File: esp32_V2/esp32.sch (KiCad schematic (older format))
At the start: 71 parts, among them IC1 KF33BD-TR, J1 USB_C, J2 Conn_01x26, J3 Conn_01x26, J4 pH, J5 ORP, Q2 8205A, Q3 BC817, Q4 BC817, SW1 Reset, SW2 Boot, U1 CH340G, U2 TC4056, U3 DW01A, U4 LM358, U5 TLC272, U6 LM358, X1 12 MHz

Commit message: Remove V2 folder and rename V2.1 folder to V2
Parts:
- removed IC1: KF33BD-TR, Package_SO:SO-8_3.9x4.9mm_P1.27mm, symbol KF33BDT-TR:KF33BD-TR
- added IC1: KF33BD-TR, Package_SO:SO-8_3.9x4.9mm_P1.27mm, symbol esp32-rescue:KF33BD-TR-KF33BDT-TR
- added JP10, JP11, JP13, JP6, JP9: Jumper_NO, Connector_PinSocket_2.54mm:PinSocket_1x02_P2.54mm_Vertical, symbol Device:Jumper_NO_Small
- J1: symbol USB_C_Receptacle_2.0:USB_C_Receptacle_2.0 -> esp32-rescue:USB_C_Receptacle_2.0-USB_C_Receptacle_2.0
- Q2: symbol 8205A:8205A -> esp32-rescue:8205A-8205A
- U3: symbol DW01A:DW01A -> esp32-rescue:DW01A-DW01A
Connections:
- net 28: now also JP9.1
- net 29: now also JP10.1
- net Bat: now also ESP32.6 (IO34), JP13.1; no longer ESP32.9 (IO33), R15.2, R16.1
- net GND: now also IC1.2 (GND), IC1.3 (GND), IC1.6 (GND), IC1.7 (GND), JP10.2, JP9.2
- net Temp: now also ESP32.9 (IO33); no longer ESP32.7 (IO35)
- net VBUS: now also JP6.2; no longer J1.A4-B9 (VBUS), J1.B4-A9 (VBUS)
- net Vcc: now also JP11.2; no longer ESP32.10 (IO25)
- net pH: now also ESP32.7 (IO35); no longer ESP32.6 (IO34)
- net at C9.1, JP2.1: now also IC1.1 (Vout)
- net at C8.1, JP1.1: now also IC1.8 (Vin)
- new net: ESP32.10 (IO25), JP11.1
- new net: JP13.2, R15.2, R16.1
- new net: J1.A4-B9 (VBUS), J1.B4-A9 (VBUS), JP6.1
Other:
- moved on the sheet: R19, R26, U4B, U5B, U5C

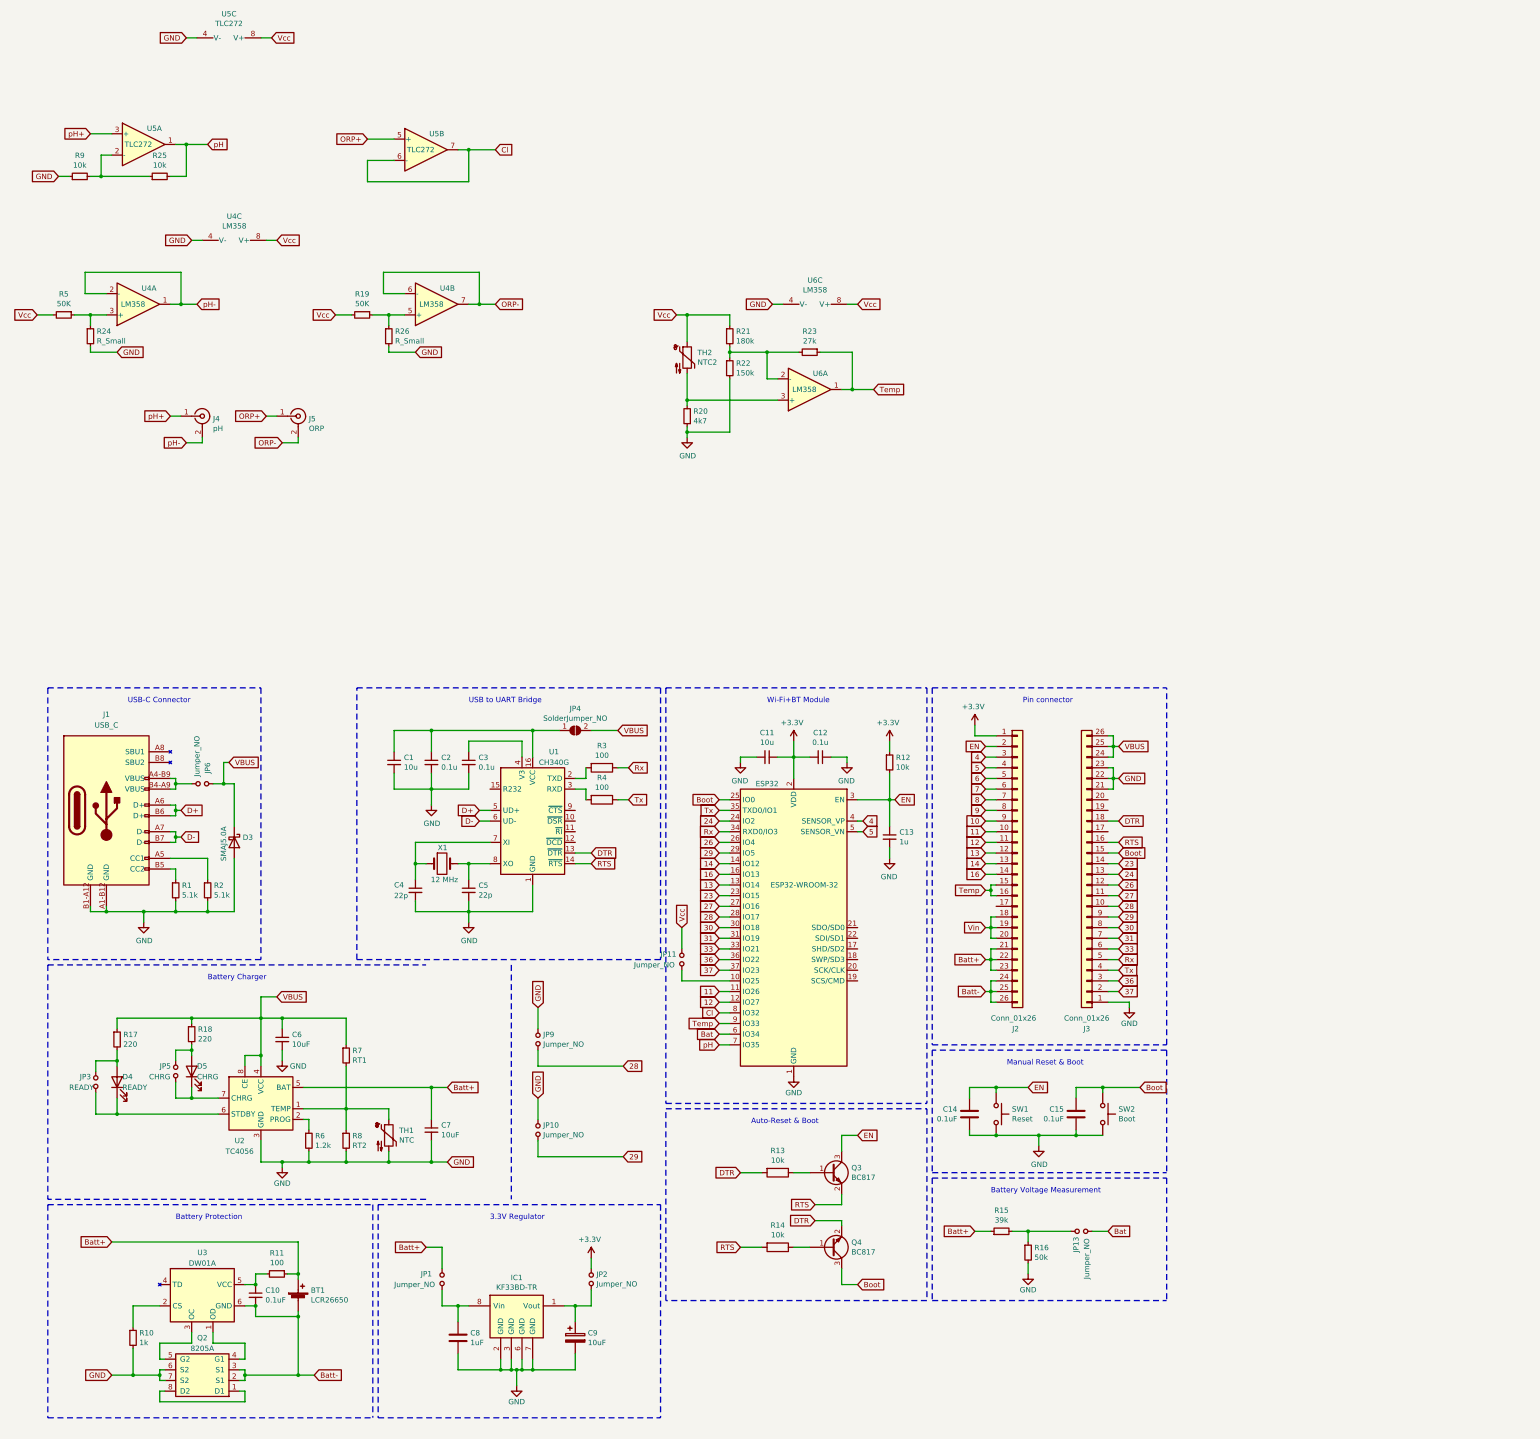
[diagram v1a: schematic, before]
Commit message: 1) Correct components values in measurement circuits - 2) Schematic cleanup - 3) Fix tracks in PCB - 4) Add Thermistor calculator
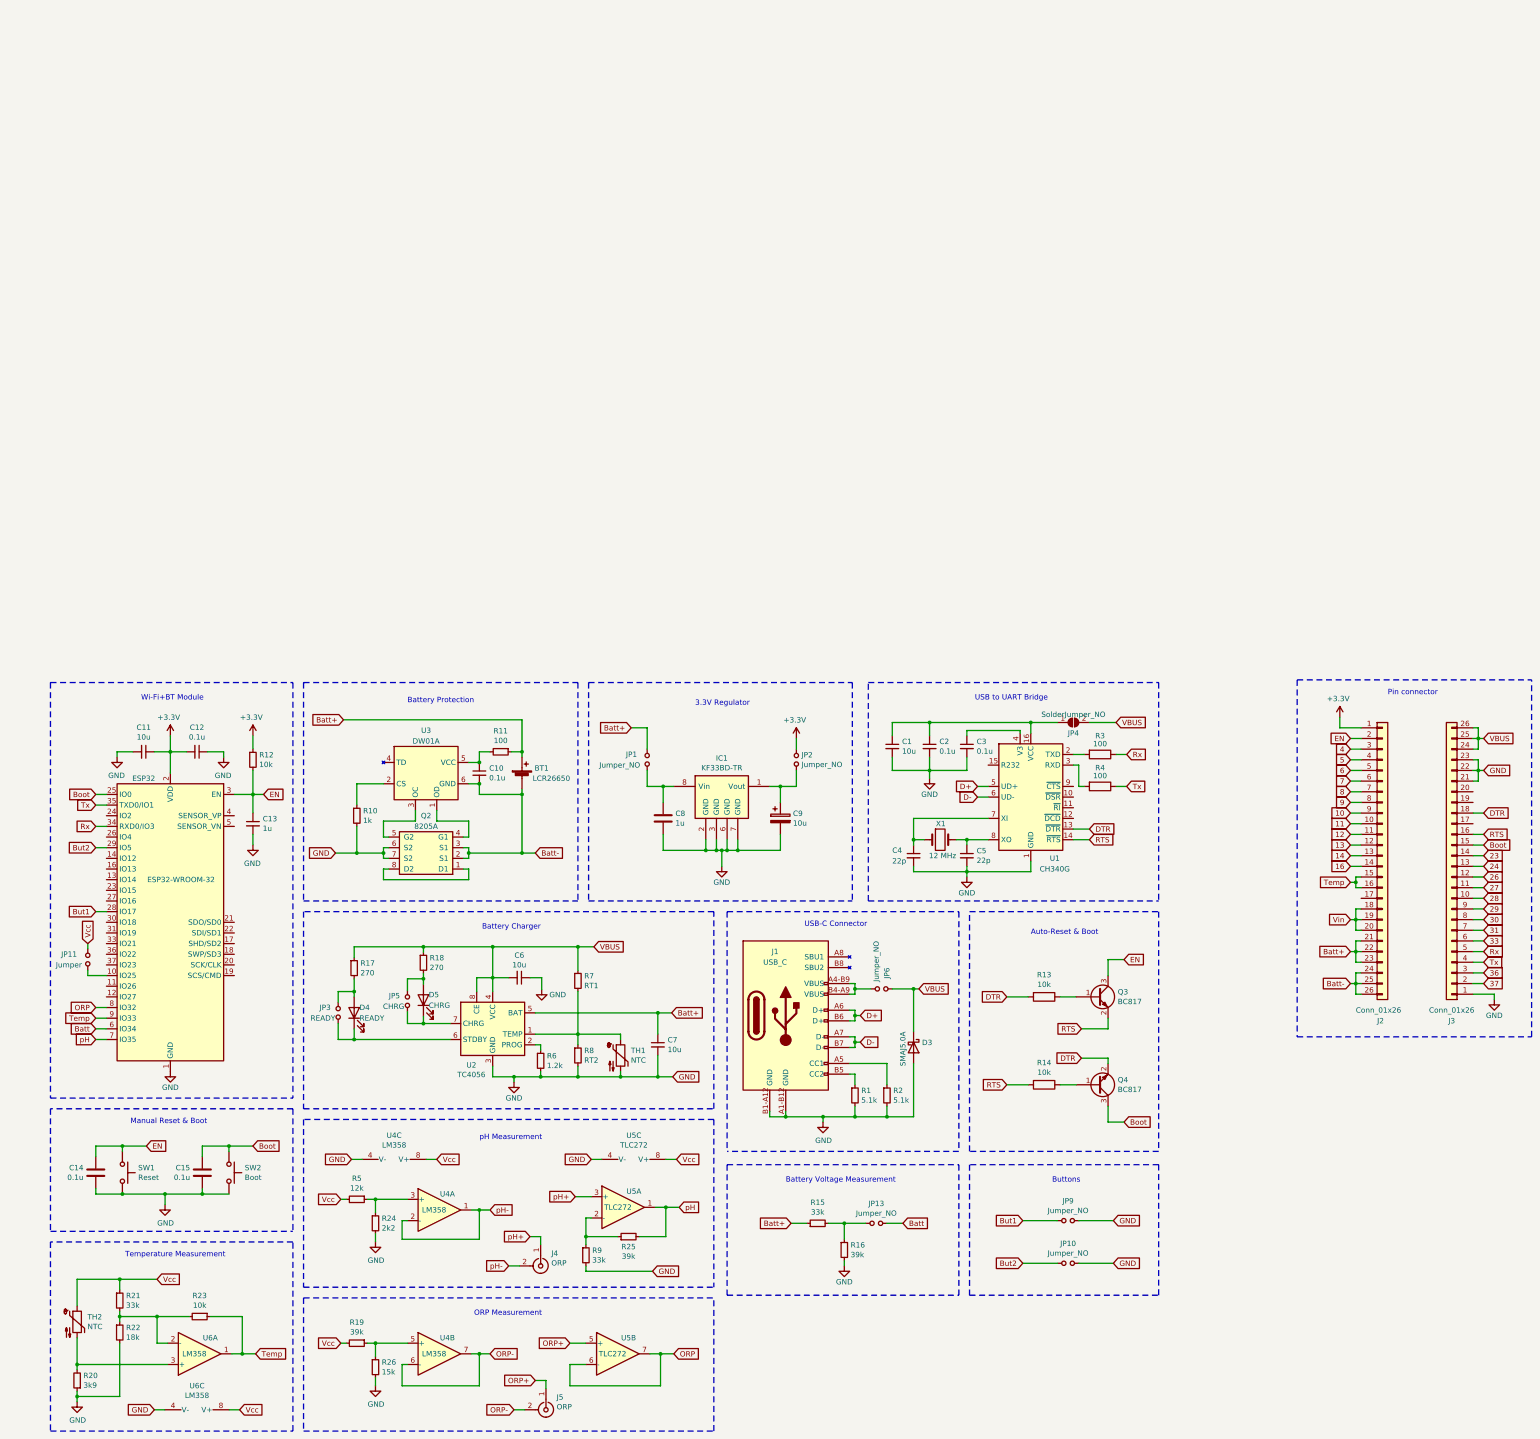
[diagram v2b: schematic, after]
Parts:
- removed unit 1 of U4
- removed unit 2 of U4
- added unit 1 of U4
- added unit 2 of U4
- C10, C14, C15: value 0.1uF -> 0.1u
- C6: value 10uF -> 10u; footprint Capacitor_SMD:C_0805_2012Metric_Pad1.15x1.40mm_HandSolder -> (none)
- C7, C9: value 10uF -> 10u
- C8: value 1uF -> 1u
- J4: value pH -> ORP; footprint Connector_Coaxial:BNC_Amphenol_B6252HB-NPP3G-50_Horizontal -> (none)
- J5: footprint Connector_Coaxial:BNC_Amphenol_B6252HB-NPP3G-50_Horizontal -> (none)
- JP10, JP13, JP9: footprint Connector_PinSocket_2.54mm:PinSocket_1x02_P2.54mm_Vertical -> (none)
- JP11: value Jumper_NO -> Jumper; footprint Connector_PinSocket_2.54mm:PinSocket_1x02_P2.54mm_Vertical -> (none)
- R15: value 39k -> 33k
- R16: value 50k -> 39k
- R17, R18: value 220 -> 270
- R19: value 50K -> 39k
- R20: value 4k7 -> 3k9
- R21: value 180k -> 33k
- R22: value 150k -> 18k
- R23: value 27k -> 10k
- R24: value R_Small -> 2k2
- R25: value 10k -> 39k
- R26: value R_Small -> 15k
- R5: value 50K -> 12k
- R9: value 10k -> 33k
- TH2: value NTC2 -> NTC
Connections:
- net 11: no longer ESP32.11 (IO26)
- net 12: no longer ESP32.12 (IO27)
- net 13: no longer ESP32.13 (IO14)
- net 14: no longer ESP32.14 (IO12)
- net 16: no longer ESP32.16 (IO13)
- net 23: no longer ESP32.23 (IO15)
- net 24: no longer ESP32.24 (IO2)
- net 26: no longer ESP32.26 (IO4)
- net 27: no longer ESP32.27 (IO16)
- net 28: no longer ESP32.28 (IO17), JP9.1
- net 29: no longer ESP32.29 (IO5), JP10.1
- net 30: no longer ESP32.30 (IO18)
- net 31: no longer ESP32.31 (IO19)
- net 33: no longer ESP32.33 (IO21)
- net 36: no longer ESP32.36 (IO22)
- net 37: no longer ESP32.37 (IO23)
- net 4: no longer ESP32.4 (SENSOR_VP)
- net 5: no longer ESP32.5 (SENSOR_VN)
- net GND: now also C6.1, R9.2; no longer C6.2, R9.1
- net ORP-: now also U4.6 (-), U4.7
- net VBUS: now also C6.2; no longer C6.1
- net pH-: now also U4.1, U4.2 (-)
- net at R15.2, R16.1: now also JP13.1; no longer JP13.2
- net at R25.1, U5.2 (-): now also R9.1; no longer R9.2
- net at R24.1, R5.1: now also U4.3 (+)
- net at R19.1, R26.1: now also U4.5 (+)
- net Bat renamed Batt
- net Batt: now also JP13.2; no longer JP13.1
- net Cl renamed ORP
- new net But1: ESP32.28 (IO17), JP9.1
- new net But2: ESP32.29 (IO5), JP10.1
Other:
- note added: "Buttons"
- note added: "ORP Measurement"
- note added: "Temperature Measurement"
- note added: "pH Measurement"
- moved on the sheet: BT1, C1, C10, C11, C12, C13, C14, C15, C2, C3, C4, C5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
